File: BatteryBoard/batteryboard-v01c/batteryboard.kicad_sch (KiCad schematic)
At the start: 36 parts, among them J1 KEYSTONE-1042, J2 KEYSTONE-1042, J3 KEYSTONE-1042, J4 KEYSTONE-1042, J5 KEYSTONE-1042, J6 KEYSTONE-1042, J7 MOLEX 5023520801, J8 Screw_Terminal_01x02, Q1 IRF7458, Q2 IRF7458, Q3 IRLML2803, Q4 IRLML2803, Q5 IRF7404TRPBF, U1 R5460N233AF

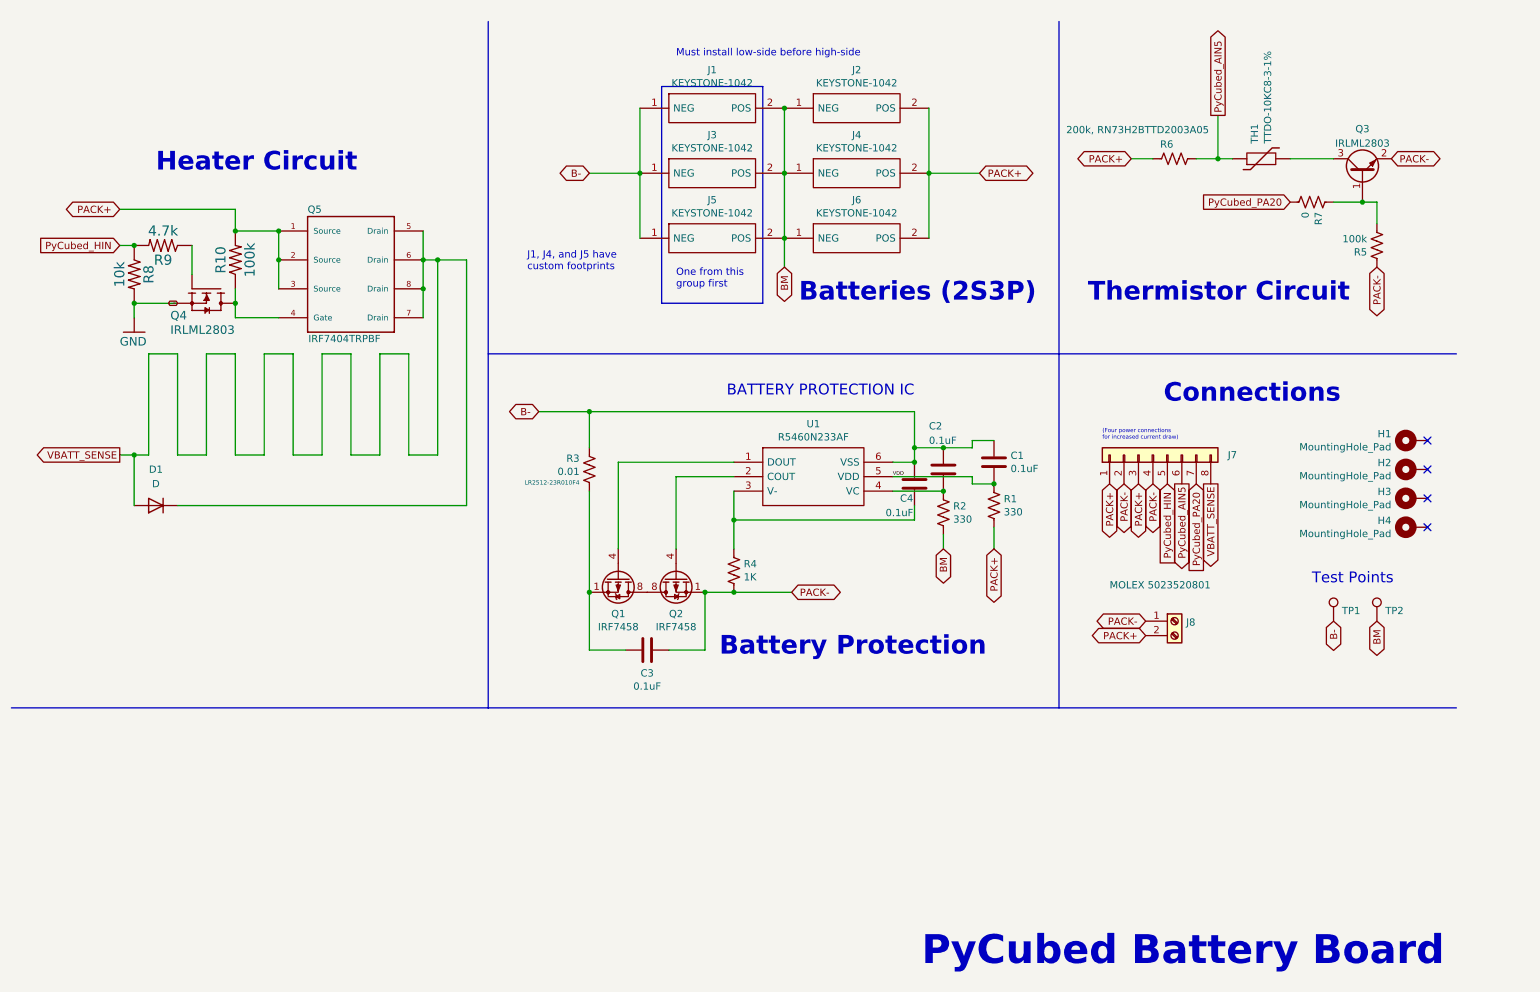
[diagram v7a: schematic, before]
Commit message: Added 3 pins to battery board, connected thermal circuit to current sense
Reverted battery board back to original (without the coulomb counter), added thermal circuit input from pycubed

Battery -> battery protection -> coulomb counter -> thermal circuit
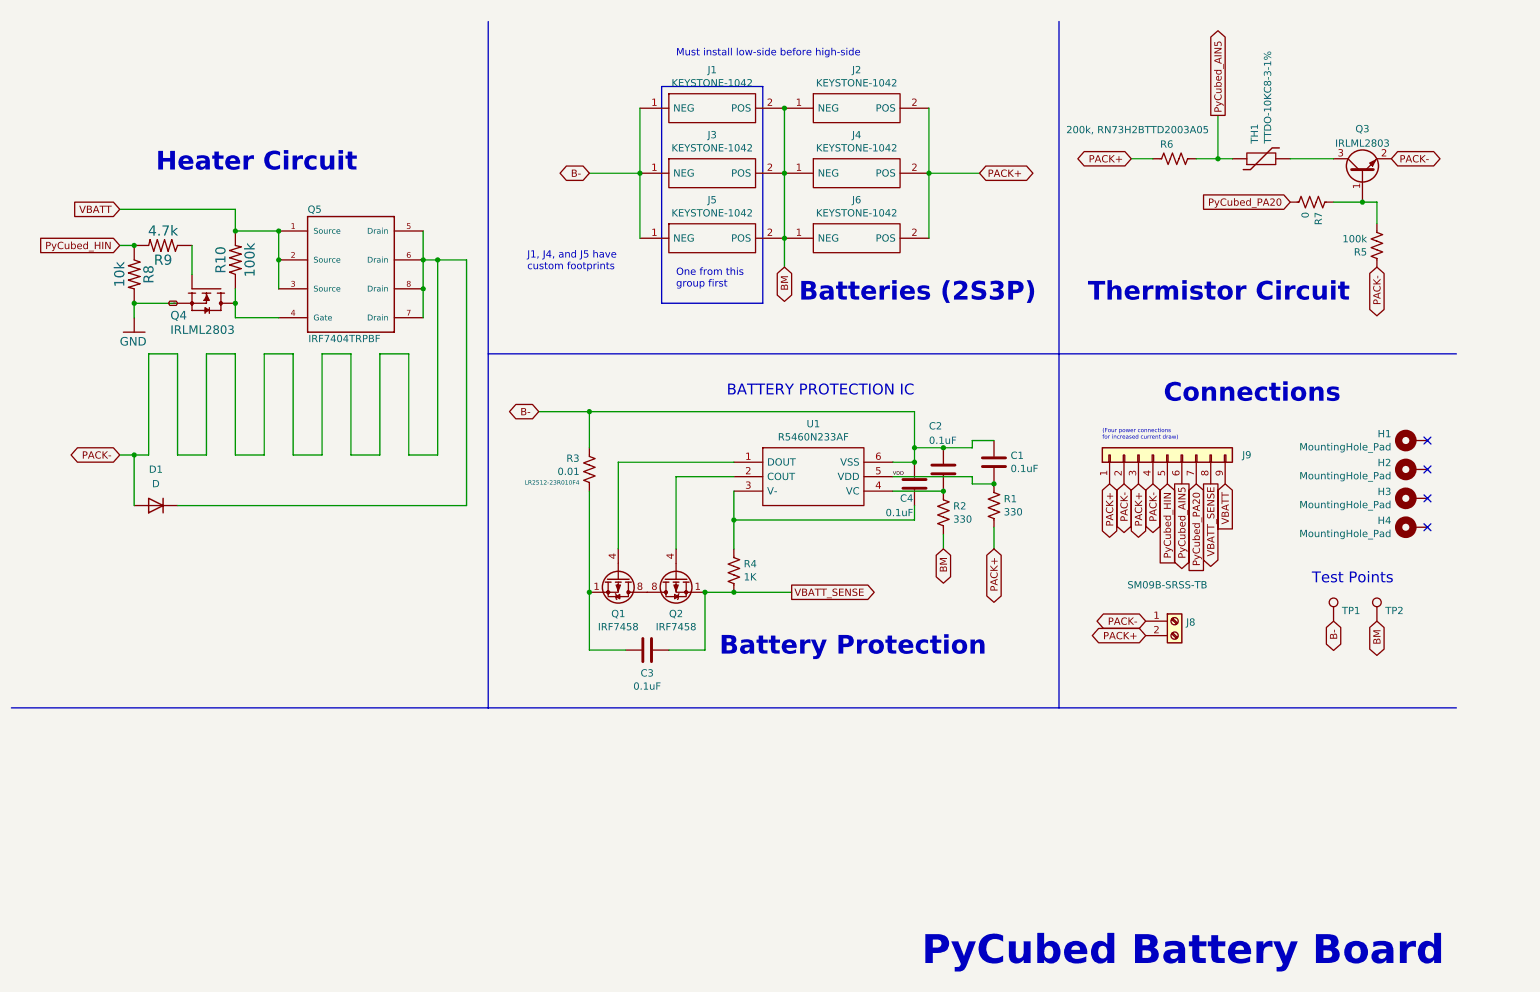
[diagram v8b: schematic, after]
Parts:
- removed J7: MOLEX 5023520801, batteryboard_local:CONN_502352-0801_MOL, symbol Connector_Generic:Conn_01x08
- added J9: SM09B-SRSS-TB, batteryboard_local:CONN9_TBLFSN_JST, symbol Connector_Generic:Conn_01x09
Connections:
- net PACK+: now also J9.1 (Pin_1), J9.3 (Pin_3); no longer Q5.1 (Source), Q5.2 (Source), Q5.3 (Source), R10.2
- net PACK-: now also D1.1 (K), D1.2 (A), Q5.5 (Drain), Q5.6 (Drain), Q5.7 (Drain), Q5.8 (Drain), J9.2 (Pin_2), J9.4 (Pin_4); no longer C3.2, Q2.1 (S), Q2.2 (S), Q2.3 (S), R4.2
- net PyCubed_AIN5: now also J9.6 (Pin_6)
- net PyCubed_HIN: now also J9.5 (Pin_5)
- net PyCubed_PA20: now also J9.7 (Pin_7)
- net VBATT_SENSE: now also C3.2, Q2.1 (S), Q2.2 (S), Q2.3 (S), R4.2, J9.8 (Pin_8); no longer D1.1 (K), D1.2 (A), Q5.5 (Drain), Q5.6 (Drain), Q5.7 (Drain), Q5.8 (Drain)
- new net VBATT: J9.9 (Pin_9), Q5.1 (Source), Q5.2 (Source), Q5.3 (Source), R10.2
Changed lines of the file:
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@@
+    )
+  )
+  (global_label "VBATT" (shape input) (at 226.06 95.25 270) (fields_autoplaced)
+    (effects (font (size 1.27 1.27)) (justify right))
+    (property "Intersheetrefs" "${INTERSHEET_REFS}" (at 226.06 102.9634 90)
+      (effects (font (size 1.27 1.27)) (justify right) hide)
     )
   )
@@
     )
   )
-  (global_label "PACK+" (shape bidirectional) (at 31.75 46.99 180) (fields_autoplaced)
-    (effects (font (size 1.27 1.27)) (justify right))
-    (property "Intersheetrefs" "${INTERSHEET_REFS}" (at 21.9955 46.99 0)
+  (global_label "VBATT" (shape input) (at 31.75 46.99 180) (fields_autoplaced)
+    (effects (font (size 1.27 1.27)) (justify right))
+    (property "Intersheetrefs" "${INTERSHEET_REFS}" (at 24.0366 46.99 0)
       (effects (font (size 1.27 1.27)) (justify right) hide)
     )
@@
     )
   )
-  (global_label "PACK-" (shape bidirectional) (at 149.86 114.3 0) (fields_autoplaced)
+  (global_label "VBATT_SENSE" (shape output) (at 149.86 114.3 0) (fields_autoplaced)
     (effects (font (size 1.27 1.27)) (justify left))
-    (property "Intersheetrefs" "${INTERSHEET_REFS}" (at 159.5351 114.3 0)
+    (property "Intersheetrefs" "${INTERSHEET_REFS}" (at 164.5885 114.3 0)
       (effects (font (size 1.27 1.27)) (justify left) hide)
     )
@@
     )
   )
+  (global_label "PACK-" (shape bidirectional) (at 31.75 90.17 180) (fields_autoplaced)
+    (effects (font (size 1.27 1.27)) (justify right))
+    (property "Intersheetrefs" "${INTERSHEET_REFS}" (at 21.9955 90.17 0)
+      (effects (font (size 1.27 1.27)) (justify right) hide)
+    )
+  )
   (global_label "PyCubed_HIN" (shape input) (at 31.75 53.34 180) (fields_autoplaced)
     (effects (font (size 1.27 1.27)) (justify right))
@@
     (effects (font (size 1.27 1.27)) (justify right))
     (property "Intersheetrefs" "${INTERSHEET_REFS}" (at 223.52 109.9785 90)
-      (effects (font (size 1.27 1.27)) (justify right) hide)
-    )
-  )
-  (global_label "VBATT_SENSE" (shape output) (at 31.75 90.17 180) (fields_autoplaced)
-    (effects (font (size 1.27 1.27)) (justify right))
-    (property "Intersheetrefs" "${INTERSHEET_REFS}" (at 17.0215 90.17 0)
       (effects (font (size 1.27 1.27)) (justify right) hide)
     )
@@
     )
   )
-  (symbol (lib_id "Connector_Generic:Conn_01x08") (at 213.36 90.17 90) (unit 1)
-    (in_bom yes) (on_board yes) (dnp no)
-    (property "Reference" "J7" (at 227.33 90.17 90)
-      (effects (font (size 1.27 1.27)))
-    )
-    (property "Value" "MOLEX 5023520801" (at 214.63 113.03 90)
-      (effects (font (size 1.27 1.27)))
-    )
-    (property "Footprint" "batteryboard_local:CONN_502352-0801_MOL" (at 213.36 90.17 0)
-      (effects (font (size 1.27 1.27)) hide)
-    )
-    (property "Datasheet" "https://tools.molex.com/pdm_docs/ps/PS-502351-001.pdf" (at 213.36 90.17 0)
+  (symbol (lib_id "Connector_Generic:Conn_01x09") (at 215.9 90.17 90) (unit 1)
+    (in_bom yes) (on_board yes) (dnp no)
+    (property "Reference" "J9" (at 229.87 90.17 90)
+      (effects (font (size 1.27 1.27)))
+    )
+    (property "Value" "SM09B-SRSS-TB" (at 215.9 113.03 90)
+      (effects (font (size 1.27 1.27)))
+    )
+    (property "Footprint" "batteryboard_local:CONN9_TBLFSN_JST" (at 215.9 90.17 0)
+      (effects (font (size 1.27 1.27)) hide)
+    )
+    (property "Datasheet" "https://www.jst-mfg.com/product/pdf/eng/eSH.pdf" (at 215.9 90.17 0)
       (effects (font (size 1.27 1.27)) hide)
     )
@@
     (pin "7")
     (pin "8")
-    (instances
-      (project "batteryboard"
-        (path "/4311e62b-bfdb-4997-ad9b-6c1b8542881a"
-          (reference "J7") (unit 1)
-        )
-      )
+    (pin "9")
+    (instances
+      (project "batteryboard"
+        (path "/4311e62b-bfdb-4997-ad9b-6c1b8542881a"
+          (reference "J9") (unit 1)
+        )
+      )
